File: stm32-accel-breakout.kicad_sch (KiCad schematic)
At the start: 38 parts, among them J1 USB_C_Receptacle_USB2.0, J2 JST-PH-01x05, J3 Conn_01x03, J5 Conn_01x04, U1 STM32F103C8Tx, U2 AP2112K-3.3, Y1 Crystal_GND24

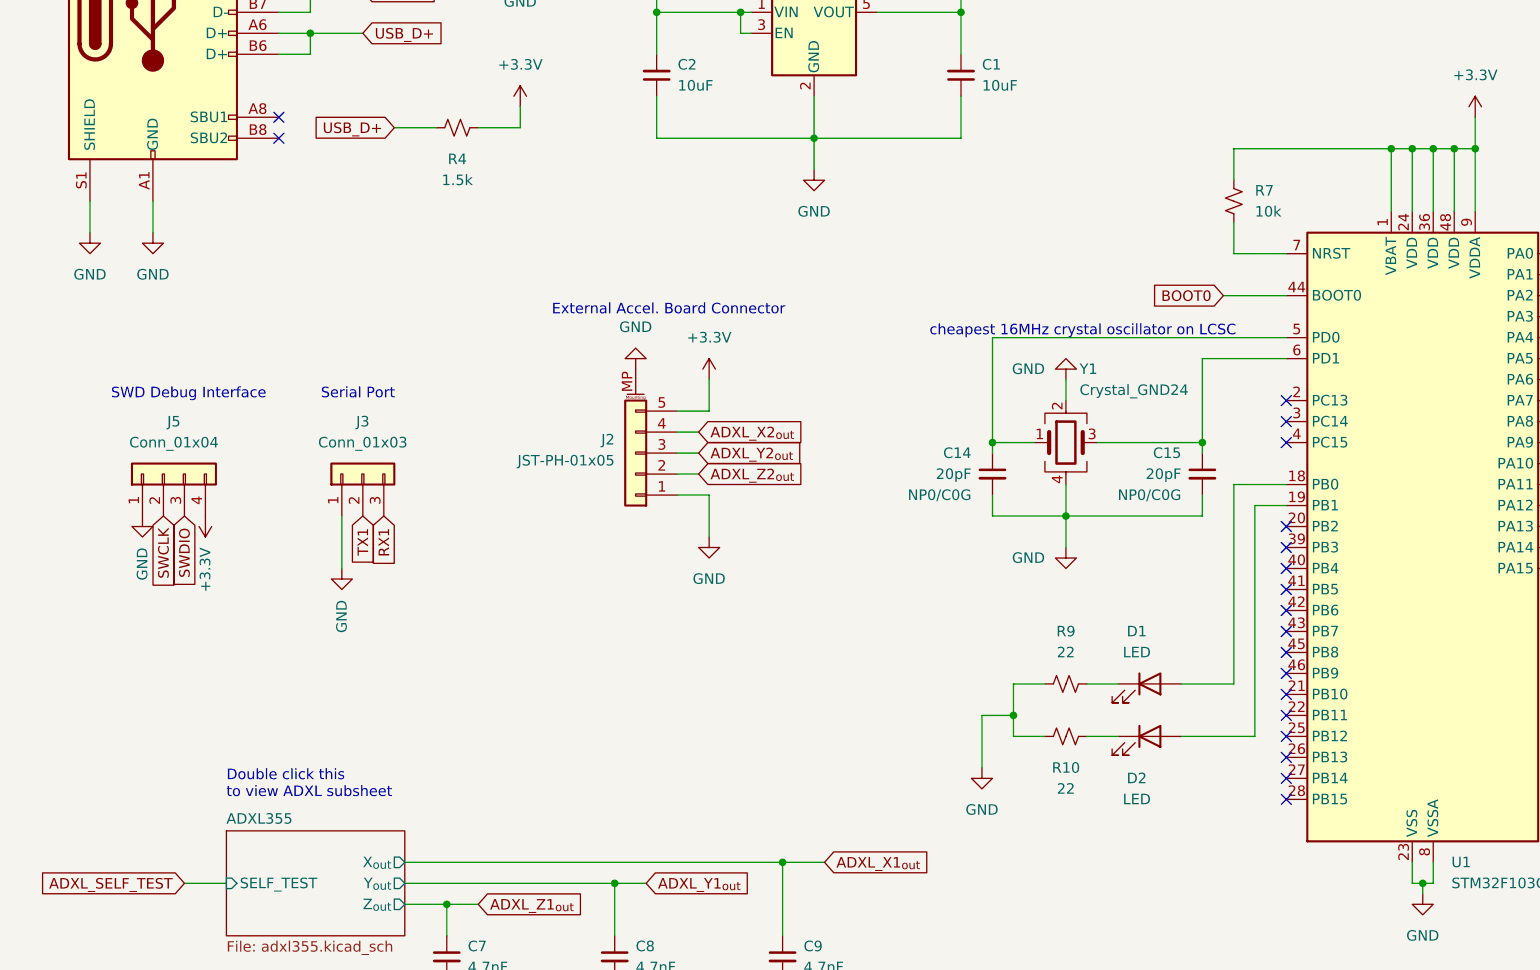
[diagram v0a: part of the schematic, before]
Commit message: changed programming header to tag connect
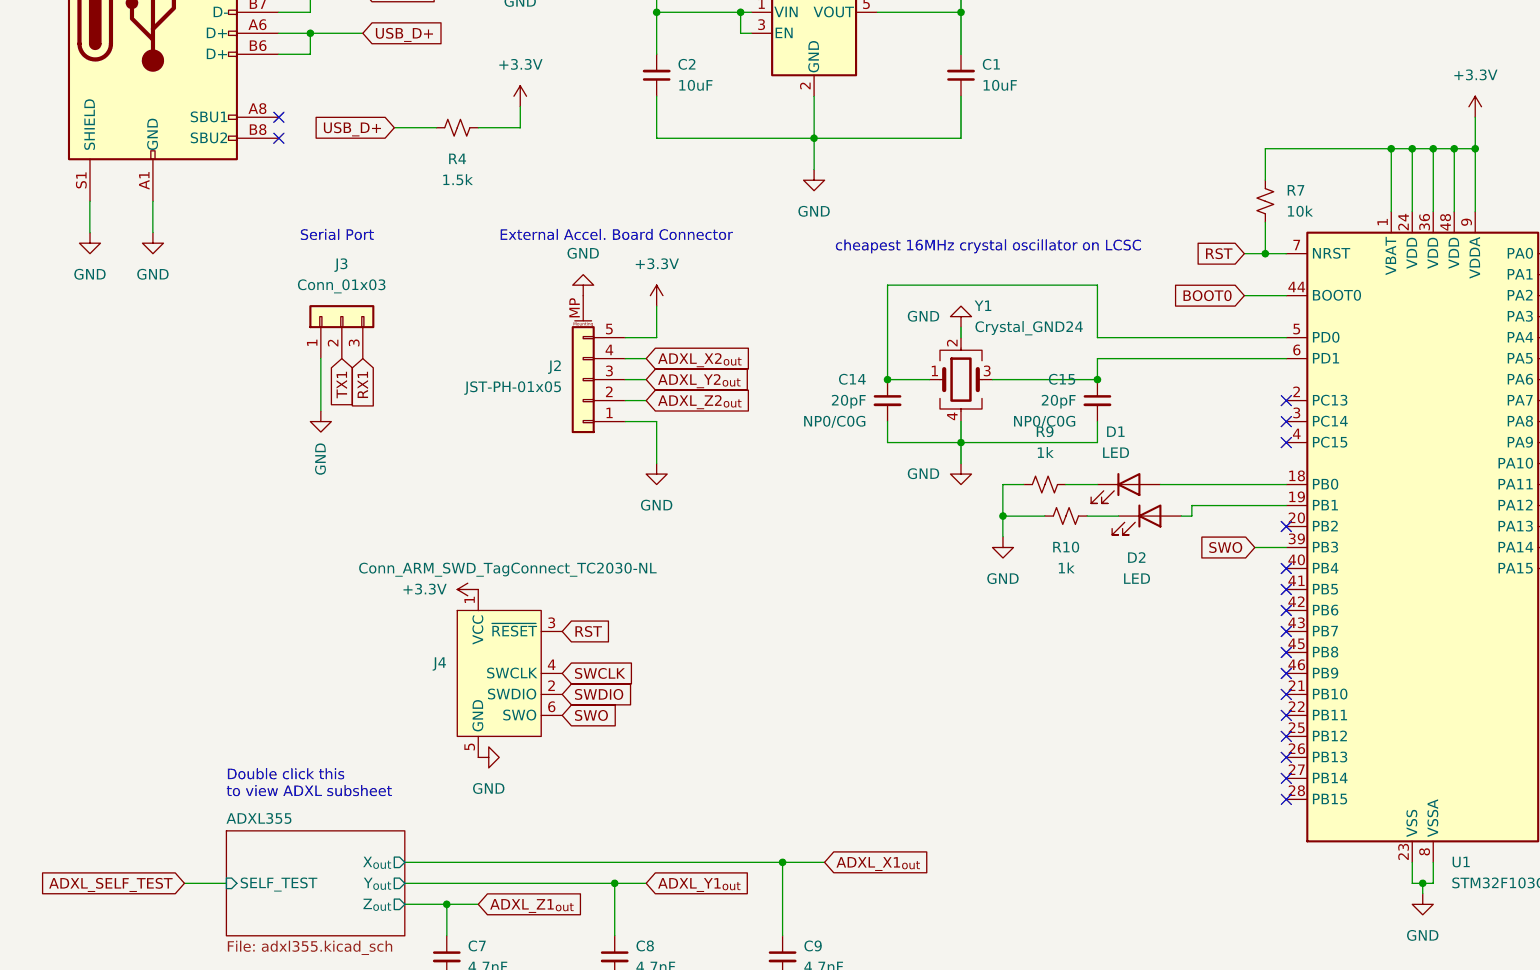
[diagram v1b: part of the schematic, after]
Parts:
- removed J5: Conn_01x04, Connector_PinHeader_2.54mm:PinHeader_1x04_P2.54mm_Horizontal, symbol Connector_Generic:Conn_01x04
- added J4: Conn_ARM_SWD_TagConnect_TC2030-NL, Connector:Tag-Connect_TC2030-IDC-NL_2x03_P1.27mm_Vertical, symbol Connector:Conn_ARM_SWD_TagConnect_TC2030-NL
- R10, R9: value 22 -> 1k
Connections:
- net +3.3V: now also J4.1 (VCC)
- net GND: now also J4.5 (GND)
- net SWCLK: now also J4.4 (SWCLK)
- net SWDIO: now also J4.2 (SWDIO)
- net RST: now reaches R7.1, U1.7 (NRST)
- net RST: now also J4.3 (~{RESET})
- net SWO: now reaches U1.39 (PB3)
- net SWO: now also J4.6 (SWO)
- no-connect marks 23 -> 22
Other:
- note removed: "SWD Debug Interface"
- moved on the sheet: C14, C15, D1, D2, J2, J3, R10, R7, R9, Y1

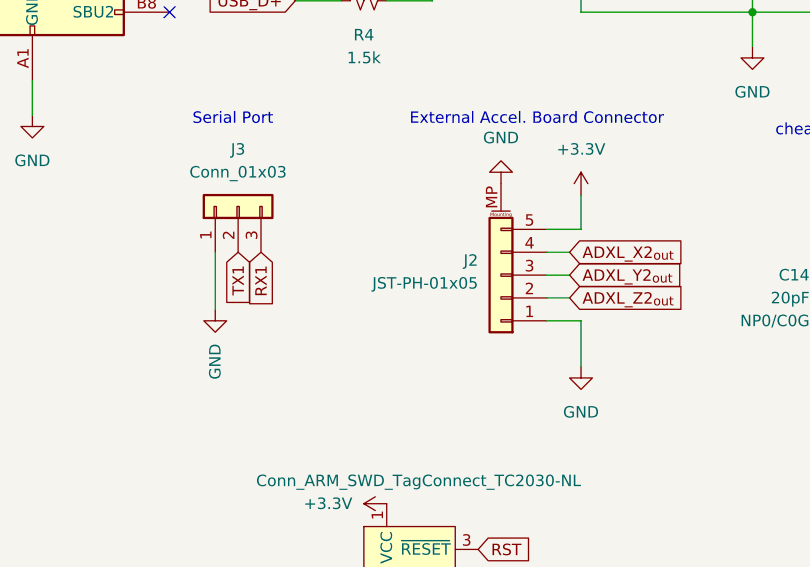
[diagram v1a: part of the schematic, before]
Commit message: changed connector for breakout accelerometer to jst-sh
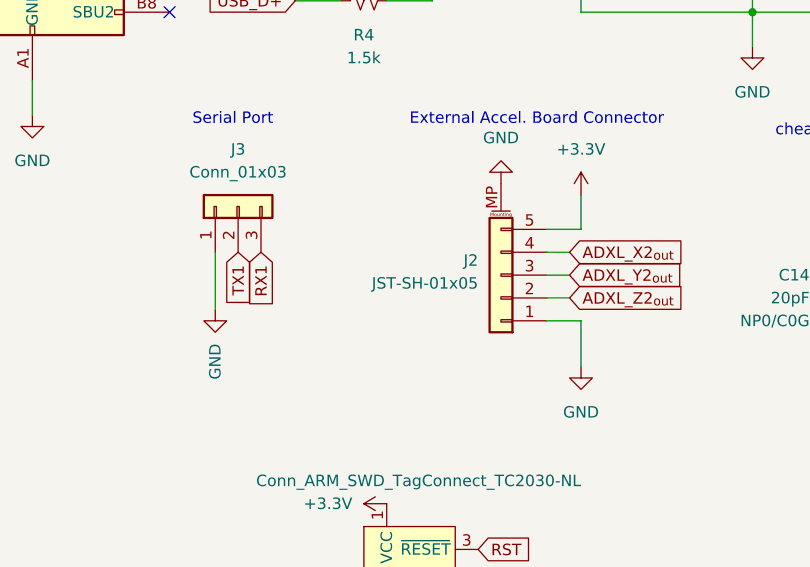
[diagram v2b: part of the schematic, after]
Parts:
- J2: value JST-PH-01x05 -> JST-SH-01x05; footprint Connector_JST:JST_PH_B5B-PH-SM4-TB_1x05-1MP_P2.00mm_Vertical -> Connector_JST:JST_SH_BM05B-SRSS-TB_1x05-1MP_P1.00mm_Vertical; LCSC C265104 -> C160391; MPN S5B-PH-SM4-TB -> BM05B-SRSS-TB(LF)(SN)
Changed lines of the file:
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@@
       (effects (font (size 1.27 1.27)) (justify left))
     )
-    (property "Value" "JST-PH-01x05" (at 78.74 93.6244 0)
+    (property "Value" "JST-SH-01x05" (at 78.74 93.6244 0)
       (effects (font (size 1.27 1.27)) (justify left))
     )
-    (property "Footprint" "Connector_JST:JST_PH_B5B-PH-SM4-TB_1x05-1MP_P2.00mm_Vertical" (at 81.28 92.71 0)
-      (effects (font (size 1.27 1.27)) hide)
-    )
-    (property "Datasheet" "https://www.jst-mfg.com/product/pdf/eng/ePH.pdf" (at 81.28 92.71 0)
-      (effects (font (size 1.27 1.27)) hide)
-    )
-    (property "LCSC" "C265104" (at 81.28 92.71 0)
-      (effects (font (size 1.27 1.27)) hide)
-    )
-    (property "MPN" "S5B-PH-SM4-TB" (at 81.28 92.71 0)
+    (property "Footprint" "Connector_JST:JST_SH_BM05B-SRSS-TB_1x05-1MP_P1.00mm_Vertical" (at 81.28 92.71 0)
+      (effects (font (size 1.27 1.27)) hide)
+    )
+    (property "Datasheet" "https://datasheet.lcsc.com/lcsc/2304140030_JST-BM05B-SRSS-TB-LF-SN_C160391.pdf" (at 81.28 92.71 0)
+      (effects (font (size 1.27 1.27)) hide)
+    )
+    (property "LCSC" "C160391" (at 81.28 92.71 0)
+      (effects (font (size 1.27 1.27)) hide)
+    )
+    (property "MPN" "BM05B-SRSS-TB(LF)(SN)" (at 81.28 92.71 0)
       (effects (font (size 1.27 1.27)) hide)
     )
@@
       (effects (font (size 1.27 1.27)) hide)
     )
+    (pin "1")
+    (pin "2")
+    (pin "3")
     (pin "4")
-    (pin "2")
+    (pin "5")
     (pin "6")
-    (pin "5")
-    (pin "1")
-    (pin "3")
-    (instances
-      (project "stm32-accel-breakout"
+    (instances
+      (project "stm32-accel-breakout"

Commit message: final edits before sending PCBs for fabrication. 10 boards ordered from JLCPCB
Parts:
- H1, H2, H3, H4, H5, H6: footprint MountingHole:MountingHole_3.2mm_M3_DIN965_Pad -> MountingHole:MountingHole_2.7mm_M2.5_DIN965_Pad
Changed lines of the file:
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@@
       (effects (font (size 1.27 1.27)) (justify left))
     )
-    (property "Footprint" "MountingHole:MountingHole_3.2mm_M3_DIN965_Pad" (at 243.84 158.75 0)
+    (property "Footprint" "MountingHole:MountingHole_2.7mm_M2.5_DIN965_Pad" (at 243.84 158.75 0)
       (effects (font (size 1.27 1.27)) hide)
     )
@@
       (effects (font (size 1.27 1.27)) (justify left))
     )
-    (property "Footprint" "MountingHole:MountingHole_3.2mm_M3_DIN965_Pad" (at 233.68 158.75 0)
+    (property "Footprint" "MountingHole:MountingHole_2.7mm_M2.5_DIN965_Pad" (at 233.68 158.75 0)
       (effects (font (size 1.27 1.27)) hide)
     )
@@
       (effects (font (size 1.27 1.27)) (justify left))
     )
-    (property "Footprint" "MountingHole:MountingHole_3.2mm_M3_DIN965_Pad" (at 259.08 158.75 0)
+    (property "Footprint" "MountingHole:MountingHole_2.7mm_M2.5_DIN965_Pad" (at 259.08 158.75 0)
       (effects (font (size 1.27 1.27)) hide)
     )
@@
       (effects (font (size 1.27 1.27)) (justify left))
     )
-    (property "Footprint" "MountingHole:MountingHole_3.2mm_M3_DIN965_Pad" (at 254 158.75 0)
+    (property "Footprint" "MountingHole:MountingHole_2.7mm_M2.5_DIN965_Pad" (at 254 158.75 0)
       (effects (font (size 1.27 1.27)) hide)
     )
@@
       (effects (font (size 1.27 1.27)) (justify left))
     )
-    (property "Footprint" "MountingHole:MountingHole_3.2mm_M3_DIN965_Pad" (at 238.76 158.75 0)
+    (property "Footprint" "MountingHole:MountingHole_2.7mm_M2.5_DIN965_Pad" (at 238.76 158.75 0)
       (effects (font (size 1.27 1.27)) hide)
     )
@@
       (effects (font (size 1.27 1.27)) (justify left))
     )
-    (property "Footprint" "MountingHole:MountingHole_3.2mm_M3_DIN965_Pad" (at 248.92 158.75 0)
-      (effects (font (size 1.27 1.27)) hide)
-    )
+    (property "Footprint" "MountingHole:MountingHole_2.7mm_M2.5_DIN965_Pad" (at 248.92 158.75 0)
+      (effects (font (size 1.27 1.27)) hide)
+    )
